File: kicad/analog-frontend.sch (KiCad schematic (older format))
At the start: 19 parts, among them J1 IRON_TIP, Q1 SIA483DJ-T1-GE3, Q2 MMBT3904, U1 ACS711xEX, U2 MCP6V71U

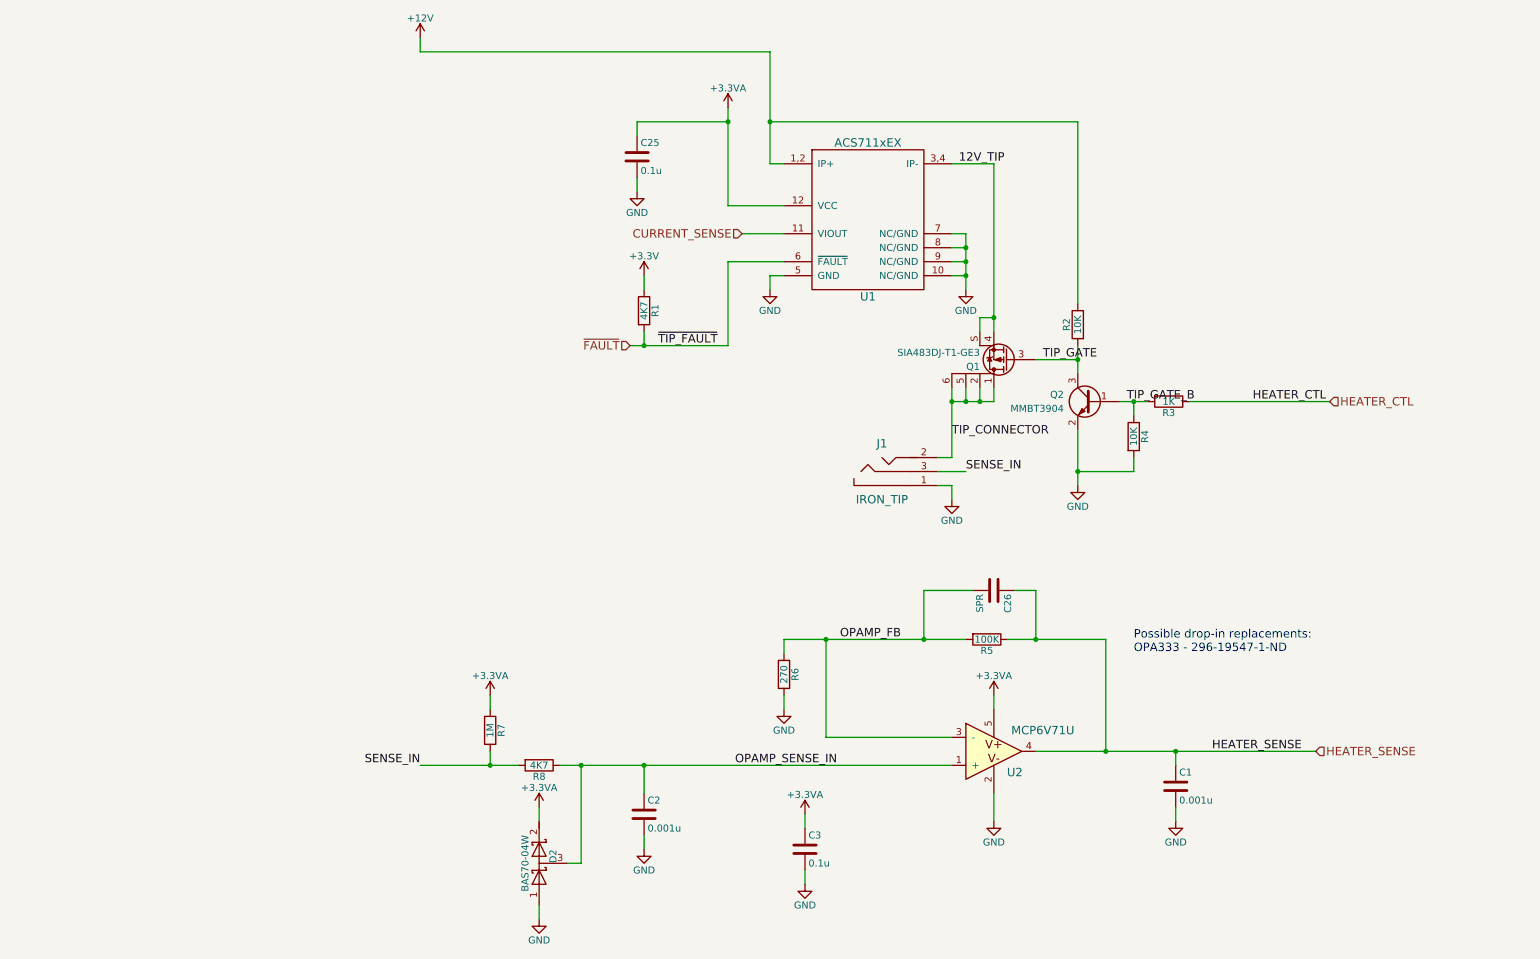
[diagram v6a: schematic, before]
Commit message: Added overtemperature latching circuit with reset
This uses a comparator to trigger the same latch type that is used on
the OVP circuit.
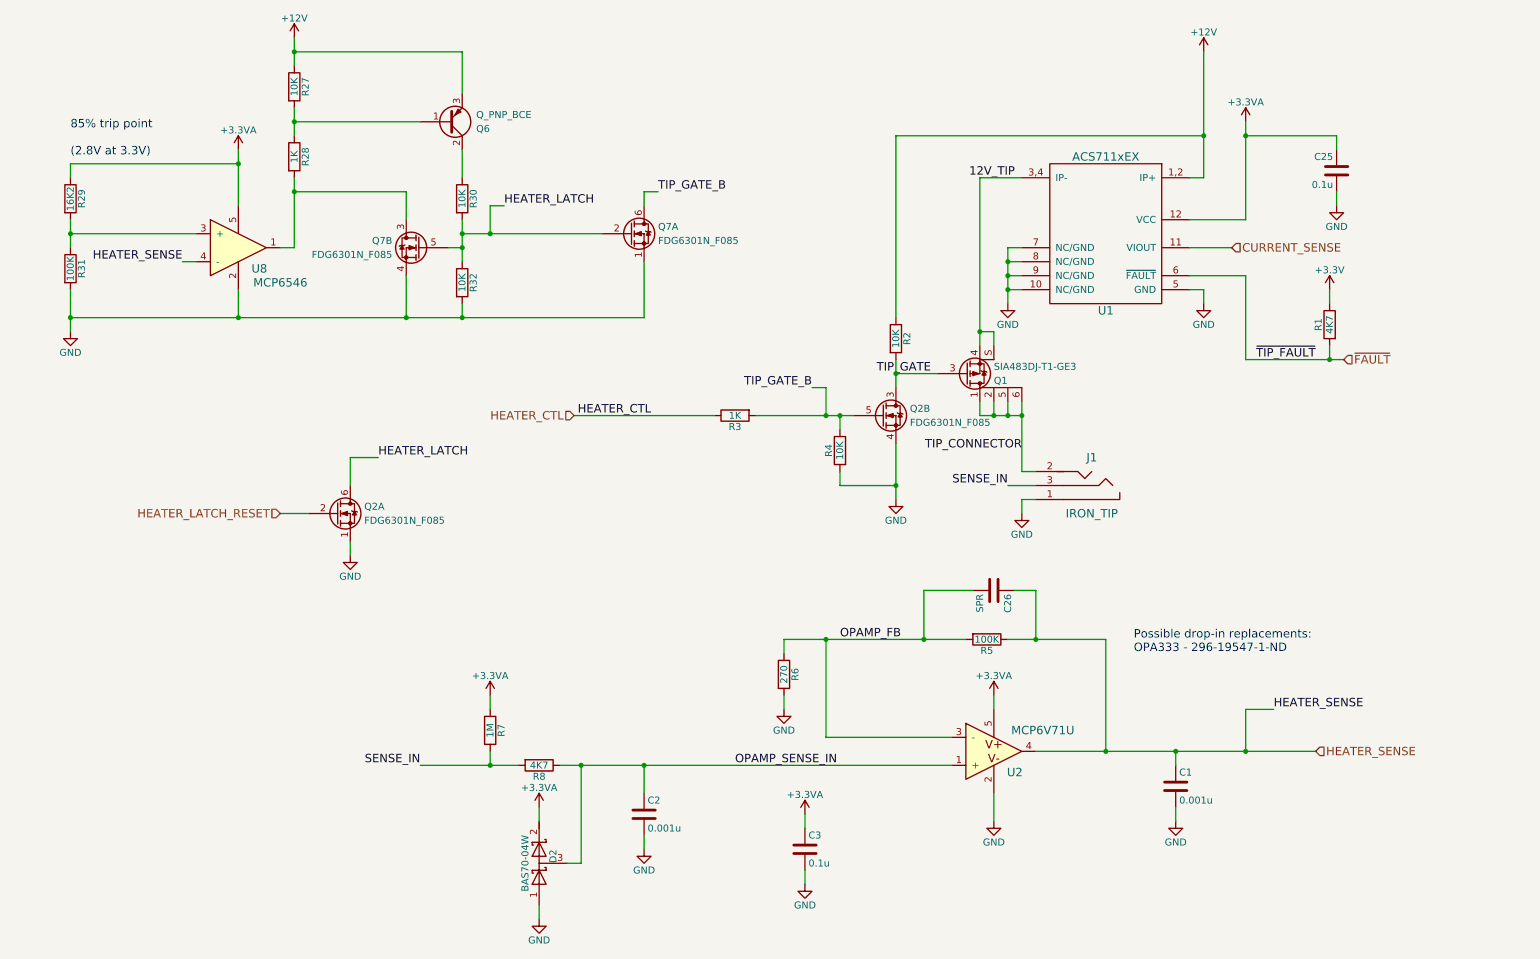
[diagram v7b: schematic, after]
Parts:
- removed Q2: MMBT3904, TO_SOT_Packages_SMD:SOT-323_SC-70, symbol Q_NPN_BEC
- added Q2, Q7: FDG6301N_F085, TO_SOT_Packages_SMD:SOT-363_SC-70-6, symbol Q_NMOS_SGD_DUAL
- added Q6: Q_PNP_BCE, symbol Q_PNP_BCE
- added R27, R30, R32: 10K, Resistors_SMD:R_0402, symbol R
- added R28: 1K, Resistors_SMD:R_0402, symbol R
- added R29: 16K2, Resistors_SMD:R_0402, symbol R
- added R31: 100K, Resistors_SMD:R_0402, symbol R
- added U8: MCP6546, TO_SOT_Packages_SMD:SOT-353_SC-70-5, symbol MCP6546
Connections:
- net +12V: now also Q6.3 (E), R27.1
- net +3.3VA: now also R29.1, U8.5
- net GND: now also Q2.1 (S), Q2.4 (S), Q7.1 (S), Q7.4 (S), R31.2, R32.2, U8.2
- net HEATER_SENSE: now also U8.4 (-)
- net TIP_GATE: now also Q2.3 (D)
- net TIP_GATE_B: now also Q2.5 (G), Q7.6 (D)
- new net: Q7.3 (D), R28.2, U8.1
- new net: Q6.1 (B), R27.2, R28.1
- new net: Q6.2 (C), R30.1
- new net: R29.2, R31.1, U8.3 (+)
- new net HEATER_LATCH: Q2.6 (D), Q7.2 (G), Q7.5 (G), R30.2, R32.1
- new net HEATER_LATCH_RESET: Q2.2 (G)
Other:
- note added: "85% trip point\n\n(2.8V at 3.3V)"
- moved on the sheet: C25, J1, Q1, R1, R2, R3, R4, U1

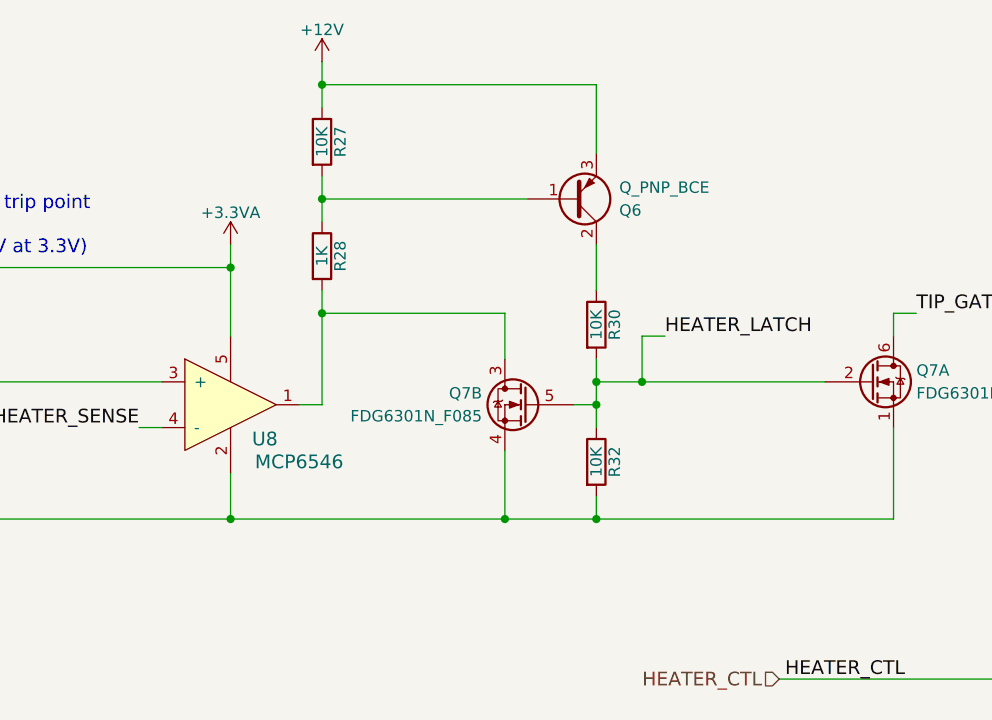
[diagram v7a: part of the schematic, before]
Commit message: Fixed thermal cutoff circuit and finished footprint selection
The main issue with the thermal cutoff was the open-collector maximum
voltage. I had to find a (slightly more expensive) comparator with an
output that was tolerant. Other comparators that would be instead
tolerant of being run off 12V were about the same price.

The fuse I'm not sure about. I'm just going to short it out. The
regulator can handle a short circuit and so can the crowbar. I also
couldn't decide where to put the feedback network. If I put it after the
fuse it would compensate for any voltage drop across it. However, it
would also cause the regulator to try to boost the voltage insanely high
during a short circuit across the fuse and maybe cause it to pop (I
could really only find ones rated to 6V). I instead placed it before the
fuse. I'm still not sure.
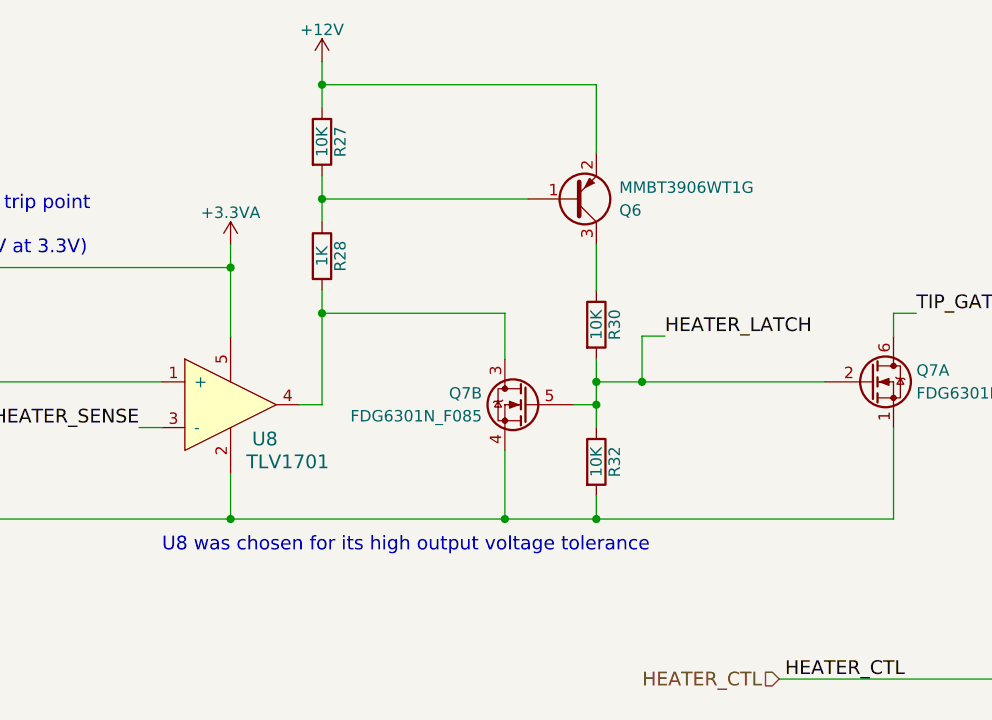
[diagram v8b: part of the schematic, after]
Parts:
- removed Q6: Q_PNP_BCE, symbol Q_PNP_BCE
- removed U8: MCP6546, TO_SOT_Packages_SMD:SOT-353_SC-70-5, symbol MCP6546
- added Q6: MMBT3906WT1G, TO_SOT_Packages_SMD:SOT-323_SC-70, symbol Q_PNP_BEC
- added U8: TLV1701, TO_SOT_Packages_SMD:SOT-353_SC-70-5, symbol TLV1701
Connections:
- net +12V: now also Q6.2 (E)
- net +3.3VA: now also U8.5
- net GND: now also U8.2
- net HEATER_SENSE: now also U8.3 (-)
- net at Q7.3 (D), R28.2: now also U8.4
- net at R27.2, R28.1: now also Q6.1 (B)
- net at R30.1: now also Q6.3 (C)
- net at R29.2, R31.1: now also U8.1 (+)
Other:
- note added: "U8 was chosen for its high output voltage tolerance"
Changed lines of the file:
@@
 	1    0    0    -1
-$EndComp
-$Comp
-L Q_PNP_BCE Q6
-U 1 1 5999E1F8
-P 3500 1300
-F 0 "Q6" H 3700 1350 50  0000 L CNN
-F 1 "Q_PNP_BCE" H 3700 1250 50  0000 L CNN
-F 2 "" H 3700 1400 50  0001 C CNN
-F 3 "" H 3500 1300 50  0001 C CNN
-	1    3500 1300
-	1    0    0    1
 $EndComp
 Text Label 1600 2300 2    60   ~ 0
@@
 Connection ~ 2000 1600
 $Comp
-L MCP6546 U8
-U 1 1 59A7C3AA
+L TLV1701 U8
+U 1 1 59A8D87F
 P 2000 2200
 F 0 "U8" H 2150 2050 60  0000 C CNN
-F 1 "MCP6546" H 2300 1950 60  0000 C CNN
+F 1 "TLV1701" H 2250 1950 60  0000 C CNN
 F 2 "TO_SOT_Packages_SMD:SOT-353_SC-70-5" H 2000 2200 60  0001 C CNN
 F 3 "" H 2000 2200 60  0001 C CNN
-F 4 "MCP6546T-I/LTCT-ND" H 2000 2200 60  0001 C CNN "Part No."
+F 4 "296-40599-1-ND" H 2000 2200 60  0001 C CNN "Part No."
 	1    2000 2200
 	1    0    0    -1
 $EndComp
+$Comp
+L Q_PNP_BEC Q6
+U 1 1 59A8DF25
+P 3500 1300
+F 0 "Q6" H 3700 1350 50  0000 L CNN
+F 1 "MMBT3906WT1G" H 3700 1250 50  0000 L CNN
+F 2 "TO_SOT_Packages_SMD:SOT-323_SC-70" H 3700 1400 50  0001 C CNN
+F 3 "" H 3500 1300 50  0001 C CNN
+F 4 "MMBT3906WT1GOSCT-ND" H 3500 1300 60  0001 C CNN "Part No."
+	1    3500 1300
+	1    0    0    1
+$EndComp
+Text Notes 1700 2850 0    60   ~ 0
+U8 was chosen for its high output voltage tolerance
 $EndSCHEMATC
